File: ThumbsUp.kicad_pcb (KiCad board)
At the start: 2 copper layers, 250.8 x 270.5 mm, 153 parts, among them IC1 RP2040, IC2 W25Q128JVSIM, IC3 RP2040, IC4 W25Q128JVSIM, J1 Conn_01x04_Male, J10 Raiser_Male, J11 Raiser_Female, J12 Raiser_Male, J13 Raiser_Female, J14 Raiser_Male, J15 Raiser_Female, J16 Raiser_Male, J17 Raiser_Female, J18 Raiser_Male, J19 Raiser_Female, J20 Conn_01x04_Female, J22 Conn_01x04_Female, J23 Conn_01x04_Female, J24 Conn_01x04_Male, J26 Conn_01x04_Male, J27 Conn_01x04_Male, J28 Conn_01x04_Female, J3 Conn_01x04_Female, J30 Conn_01x04_Female, J31 Conn_01x04_Female, J32 USB_C_Receptacle_USB2.0, J33 Raiser_Male, J34 Raiser_Female, J35 Raiser_Male, J36 STX-3501-3N, J37 USB_C_Receptacle_USB2.0, J38 Raiser_Female, J39 Raiser_Male, J4 Conn_01x04_Male, J40 Raiser_Female, J41 Raiser_Male, J42 Raiser_Female, J43 Raiser_Male, J44 Raiser_Female, J45 Raiser_Male, J46 STX-3501-3N, J47 Raiser_Female, J48 Raiser_Male, J49 Raiser_Female, J5 Conn_01x04_Female, J50 Raiser_Male, J51 Raiser_Female, J52 Raiser_Male, J6 Conn_01x04_Male, J7 Conn_01x04_Male, J8 Conn_01x04_Male, J9 Raiser_Female, U1 AMS1117-3.3_SOT223, U2 AMS1117-3.3_SOT223, Y1 ABLS-12.000MHZ-B4-T, Y2 ABLS-12.000MHZ-B4-T

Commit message: Re-wired R2 RP2040 and memory as per manual
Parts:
- moved R13 11.4 mm to (161.0, 453.7), turned to 180 degrees
- moved R12 10.9 mm to (164.1, 453.6)
- moved C19 8.45 mm to (157.4, 453.7), turned to 180 degrees
- moved C28 3.43 mm to (181.6, 461.6)
- moved R16 3.43 mm to (181.6, 459.6)
- moved C29 3.43 mm to (181.6, 460.6)
- moved C32 3.31 mm to (175.8, 453.8)
- moved IC4 3.05 mm to (160.5, 460.0), turned to 270 degrees
- moved IC3 2.85 mm to (174.6, 459.8)
- moved C27 2.73 mm to (171.6, 453.8)
- moved C21 2.65 mm to (181.6, 457.4)
- moved C22 2.65 mm to (181.6, 458.5)
- moved C23 2.17 mm to (170.2, 466.4)
- moved C31 1.62 mm to (176.3, 465.9), turned to 0 degrees
- moved C20 1.48 mm to (167.6, 459.9)
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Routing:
- net +3V3: track 235.8 -> 292.2 mm, vias 12 -> 9
- net +1V1: track 55.5 -> 85.1 mm, vias 7 -> 11
- net K_BSPC: track 71.8 -> 50.2 mm
- net L-BASE: track 836.6 -> 817.2 mm, vias 25 -> 22
- net RQSPI_SSN: track 35.5 -> 17.9 mm
- net RQSPI_SD1: track 28.8 -> 13.3 mm
- net RQSPI_SD2: track 26.3 -> 11.9 mm
- net R-TIP: track 90.5 -> 79.3 mm
- net Net-(BOOTSEL2-PadA1): track 66.1 -> 77.0 mm
- net RQSPI_SD3: track 11.0 -> 21.0 mm
- net RQSPI_SCLK: track 11.8 -> 19.3 mm
- net Net-(IC3-Pad26): track 34.5 -> 28.4 mm, vias 1 -> 2
- net RQSPI_SD0: track 13.1 -> 18.2 mm
- net K_I: track 41.2 -> 45.6 mm
- net K_O: track 38.5 -> 42.9 mm
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
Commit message: Re-wired R2 RP2040 and memory as per manual
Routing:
- net L-BASE: track 817.2 -> 828.9 mm
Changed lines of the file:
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@@
     (thickness 1.6)
     (drawings 157)
-    (tracks 1897)
+    (tracks 1902)
     (zones 0)
     (modules 153)
@@
     (34 B.Paste user)
     (35 F.Paste user)
-    (36 B.SilkS user hide)
-    (37 F.SilkS user hide)
+    (36 B.SilkS user)
+    (37 F.SilkS user)
     (38 B.Mask user)
     (39 F.Mask user)
@@
   (segment (start 162.84 465.15) (end 162.385 464.695) (width 0.2) (layer B.Cu) (net 33))
   (segment (start 171.1875 458.4375) (end 169.792425 458.4375) (width 0.2) (layer B.Cu) (net 33))
-  (segment (start 168.245452 457.352989) (end 165.524548 457.352989) (width 0.2) (layer B.Cu) (net 34))
-  (segment (start 162.512011 465.477011) (end 161.115 464.08) (width 0.2) (layer B.Cu) (net 34))
+  (segment (start 161.115 464.625) (end 161.115 463.58) (width 0.2) (layer B.Cu) (net 34))
+  (segment (start 161.967011 465.477011) (end 161.115 464.625) (width 0.2) (layer B.Cu) (net 34))
   (segment (start 171.1875 458.8375) (end 169.729963 458.8375) (width 0.2) (layer B.Cu) (net 34))
-  (segment (start 164.455452 465.477011) (end 162.512011 465.477011) (width 0.2) (layer B.Cu) (net 34))
-  (segment (start 161.115 464.08) (end 161.115 463.58) (width 0.2) (layer B.Cu) (net 34))
+  (segment (start 164.455452 465.477011) (end 161.967011 465.477011) (width 0.2) (layer B.Cu) (net 34))
   (segment (start 169.729963 458.8375) (end 168.245452 457.352989) (width 0.2) (layer B.Cu) (net 34))
+  (segment (start 168.245452 457.352989) (end 165.524548 457.352989) (width 0.2) (layer B.Cu) (net 34))
+  (segment (start 165.524548 457.352989) (end 164.647011 458.230526) (width 0.2) (layer B.Cu) (net 34))
   (segment (start 164.647011 458.230526) (end 164.647011 465.285452) (width 0.2) (layer B.Cu) (net 34))
   (segment (start 164.647011 465.285452) (end 164.455452 465.477011) (width 0.2) (layer B.Cu) (net 34))
-  (segment (start 165.524548 457.352989) (end 164.647011 458.230526) (width 0.2) (layer B.Cu) (net 34))
   (segment (start 159.845 464.645) (end 159.845 463.58) (width 0.2) (layer B.Cu) (net 35))
   (segment (start 161.004022 465.804022) (end 159.845 464.645) (width 0.2) (layer B.Cu) (net 35))
@@
   (segment (start 159.552025 432.920322) (end 160.25 433.618297) (width 0.5) (layer B.Cu) (net 43))
   (segment (start 160.25 433.618297) (end 160.25 437.05) (width 0.5) (layer B.Cu) (net 43))
-  (segment (start 186.222025 441.000322) (end 182.61 444.612347) (width 0.5) (layer B.Cu) (net 43))
-  (segment (start 182.61 444.612347) (end 182.61 447.71) (width 0.5) (layer B.Cu) (net 43))
   (segment (start 176.595 393.53) (end 176.595 392.98) (width 0.5) (layer B.Cu) (net 43))
   (segment (start 177.545 394.48) (end 176.595 393.53) (width 0.5) (layer B.Cu) (net 43))
@@
   (segment (start 182.95 458.525) (end 182.95 461.49) (width 0.5) (layer F.Cu) (net 43))
   (segment (start 182.99 461.6) (end 181.222999 463.367001) (width 0.5) (layer B.Cu) (net 43))
-  (segment (start 174.625 459.8375) (end 178.1975 463.41) (width 0.5) (layer F.Cu) (net 43))
   (via (at 179.092999 463.367001) (size 0.8) (drill 0.4) (layers F.Cu B.Cu) (net 43))
   (segment (start 179.05 463.41) (end 179.092999 463.367001) (width 0.5) (layer F.Cu) (net 43))
@@
   (segment (start 168.24 466.86) (end 166.36 464.98) (width 0.5) (layer B.Cu) (net 43))
   (segment (start 182.095 460.575) (end 182.095 461.6) (width 0.5) (layer B.Cu) (net 43))
+  (segment (start 184.912025 444.051312) (end 184.912025 442.460322) (width 0.5) (layer F.Cu) (net 43))
+  (segment (start 184.912025 446.417975) (end 184.912025 444.051312) (width 0.5) (layer F.Cu) (net 43))
+  (segment (start 176.29 451.95) (end 179.38 451.95) (width 0.5) (layer F.Cu) (net 43))
+  (segment (start 179.75 451.97) (end 179.555 451.775) (width 0.5) (layer F.Cu) (net 43))
+  (segment (start 179.75 458.525) (end 179.75 451.97) (width 0.5) (layer F.Cu) (net 43))
+  (segment (start 179.38 451.95) (end 179.555 451.775) (width 0.5) (layer F.Cu) (net 43))
+  (segment (start 179.555 451.775) (end 184.912025 446.417975) (width 0.5) (layer F.Cu) (net 43))
+  (segment (start 178.1975 463.41) (end 175.9 461.1125) (width 0.5) (layer F.Cu) (net 43))
   (segment (start 111.91 418.79) (end 111.875 418.755) (width 0.5) (layer B.Cu) (net 44))
   (segment (start 113.14 418.79) (end 111.91 418.79) (width 0.5) (layer B.Cu) (net 44))

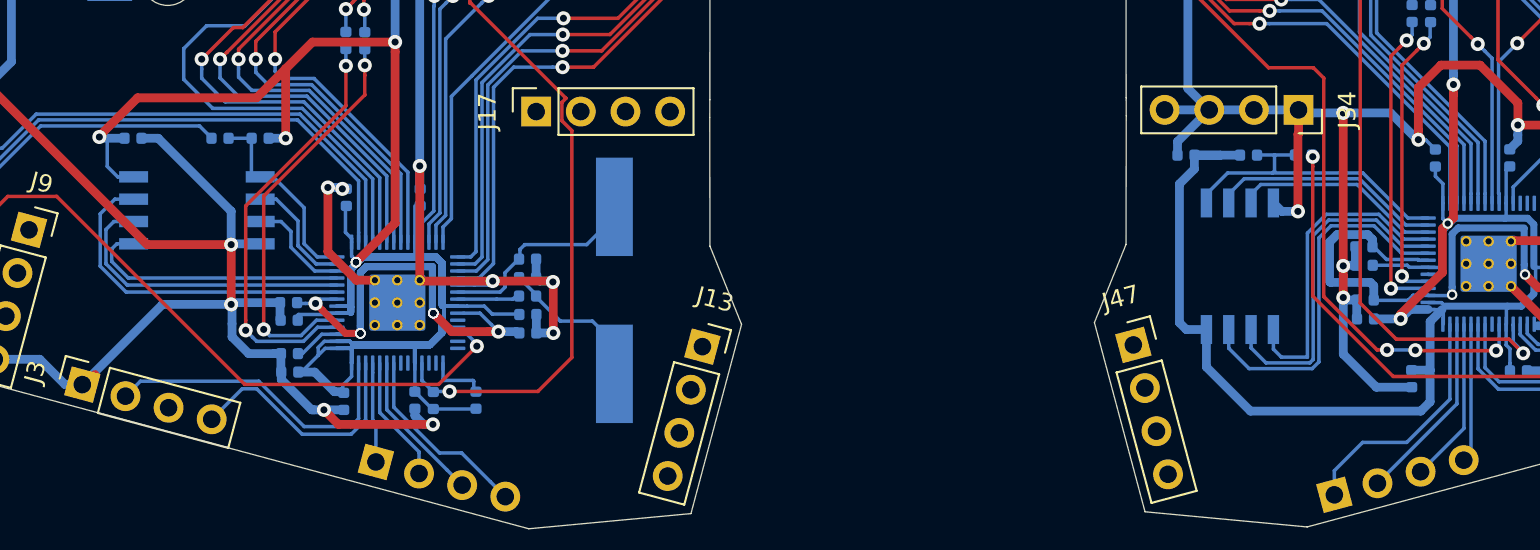
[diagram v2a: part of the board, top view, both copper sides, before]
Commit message: Re-wired R2 RP2040 - moved the R, C around it.
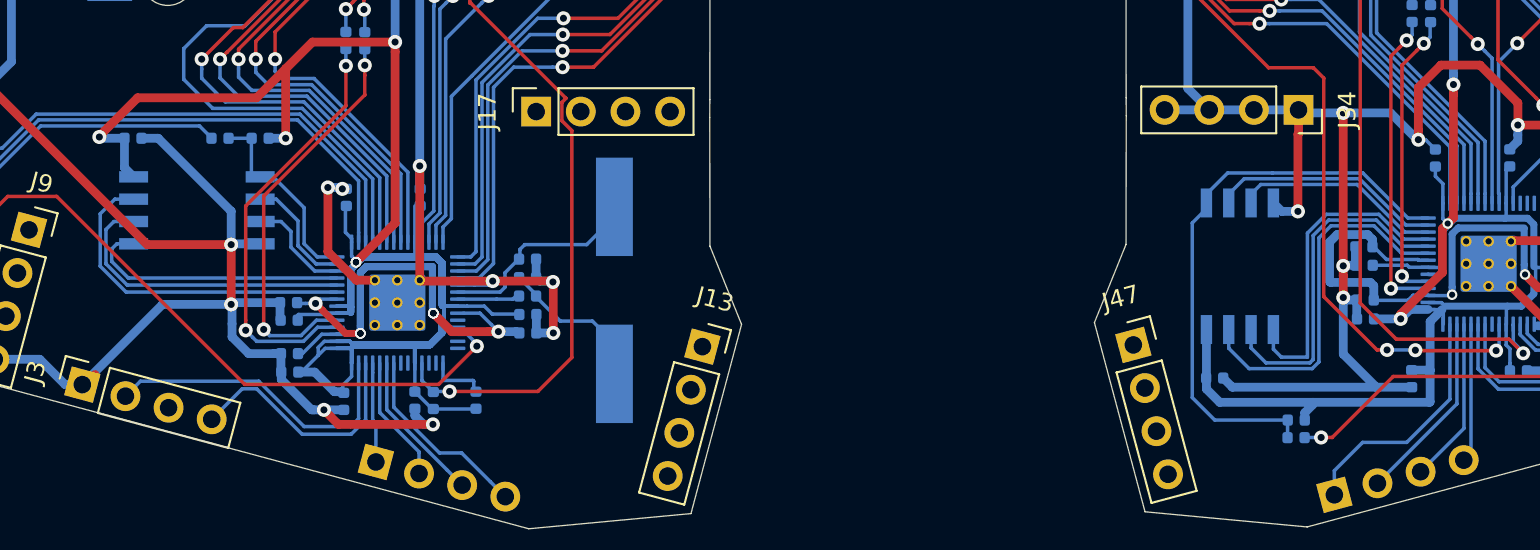
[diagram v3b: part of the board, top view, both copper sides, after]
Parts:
- moved R12 16.1 mm to (163.7, 469.7)
- moved R13 15.3 mm to (163.7, 468.7), turned to 0 degrees
- moved C19 12.8 mm to (159.0, 466.3), turned to 0 degrees
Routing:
- net RQSPI_SSN: track 17.9 -> 33.0 mm
- net +3V3: track 292.2 -> 277.2 mm
- net Net-(BOOTSEL2-PadA1): track 77.0 -> 69.0 mm
- net L-BASE: track 828.9 -> 834.5 mm
